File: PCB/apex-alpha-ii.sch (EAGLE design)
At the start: 31 parts, among them IC1 CC430F5135, X2 SMA-142-0701-801/806, Y1 26MHz

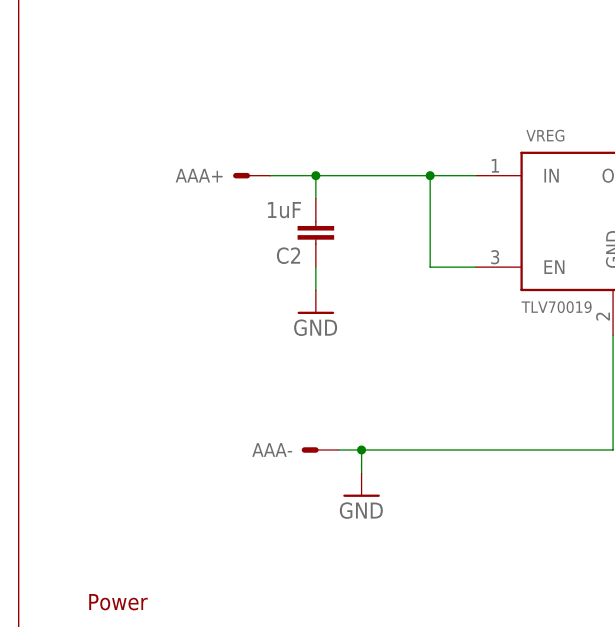
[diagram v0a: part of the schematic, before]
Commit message: Replaced AAA holder with CR123A holder
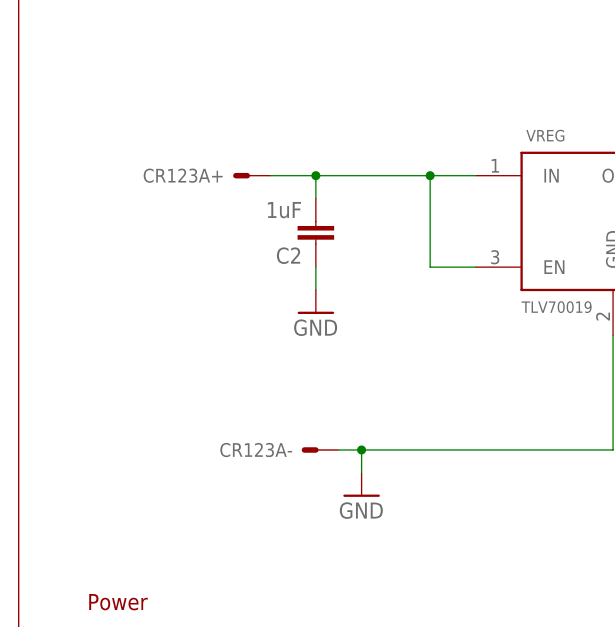
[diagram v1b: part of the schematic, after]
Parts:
- removed AAA: SMD-BATTERY-HOLDER-AAA, apex:SMD-BATTERY-HOLDER-AAA
- added CR123A: SMD-BATTERY-HOLDER-CR123A, apex:SMD-BATTERY-HOLDER-CR123A
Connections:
- net GND: now also CR123A-.S; no longer AAA-.S
- net N$3: now also CR123A+.S; no longer AAA+.S
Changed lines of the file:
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@@
 <part name="U$1" library="Ava" deviceset="JTI_ANTENNA-1575AT43A40" device=""/>
 <part name="GND1" library="apex" deviceset="GND" device=""/>
-<part name="AAA" library="apex" deviceset="SMD-BATTERY-HOLDER-AAA" device="" value=""/>
+<part name="CR123A" library="apex" deviceset="SMD-BATTERY-HOLDER-CR123A" device="" value=""/>
 <part name="GND2" library="apex" deviceset="GND" device=""/>
 <part name="C2" library="apex" deviceset="CAP" device="0402-CAP" value="1uF"/>
@@
 <instance part="U$1" gate="G$1" x="68.58" y="129.54" rot="R90"/>
 <instance part="GND1" gate="1" x="134.62" y="185.42"/>
-<instance part="AAA" gate="+" x="76.2" y="200.66" rot="R180"/>
-<instance part="AAA" gate="-" x="83.82" y="170.18" rot="R180"/>
+<instance part="CR123A" gate="+" x="76.2" y="200.66" rot="R180"/>
+<instance part="CR123A" gate="-" x="83.82" y="170.18" rot="R180"/>
 <instance part="GND2" gate="1" x="88.9" y="165.1"/>
 <instance part="C2" gate="G$1" x="83.82" y="195.58" rot="R180"/>
@@
 <net name="GND" class="0">
 <segment>
-<pinref part="AAA" gate="-" pin="S"/>
+<pinref part="CR123A" gate="-" pin="S"/>
 <wire x1="86.36" y1="170.18" x2="88.9" y2="170.18" width="0.1524" layer="91"/>
 <wire x1="88.9" y1="170.18" x2="88.9" y2="167.64" width="0.1524" layer="91"/>
@@
 <pinref part="C2" gate="G$1" pin="2"/>
 <wire x1="83.82" y1="198.12" x2="83.82" y2="200.66" width="0.1524" layer="91"/>
-<pinref part="AAA" gate="+" pin="S"/>
+<pinref part="CR123A" gate="+" pin="S"/>
 <wire x1="78.74" y1="200.66" x2="83.82" y2="200.66" width="0.1524" layer="91"/>
 <pinref part="VREG" gate="G$1" pin="IN"/>
